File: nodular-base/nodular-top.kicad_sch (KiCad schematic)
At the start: 0 parts

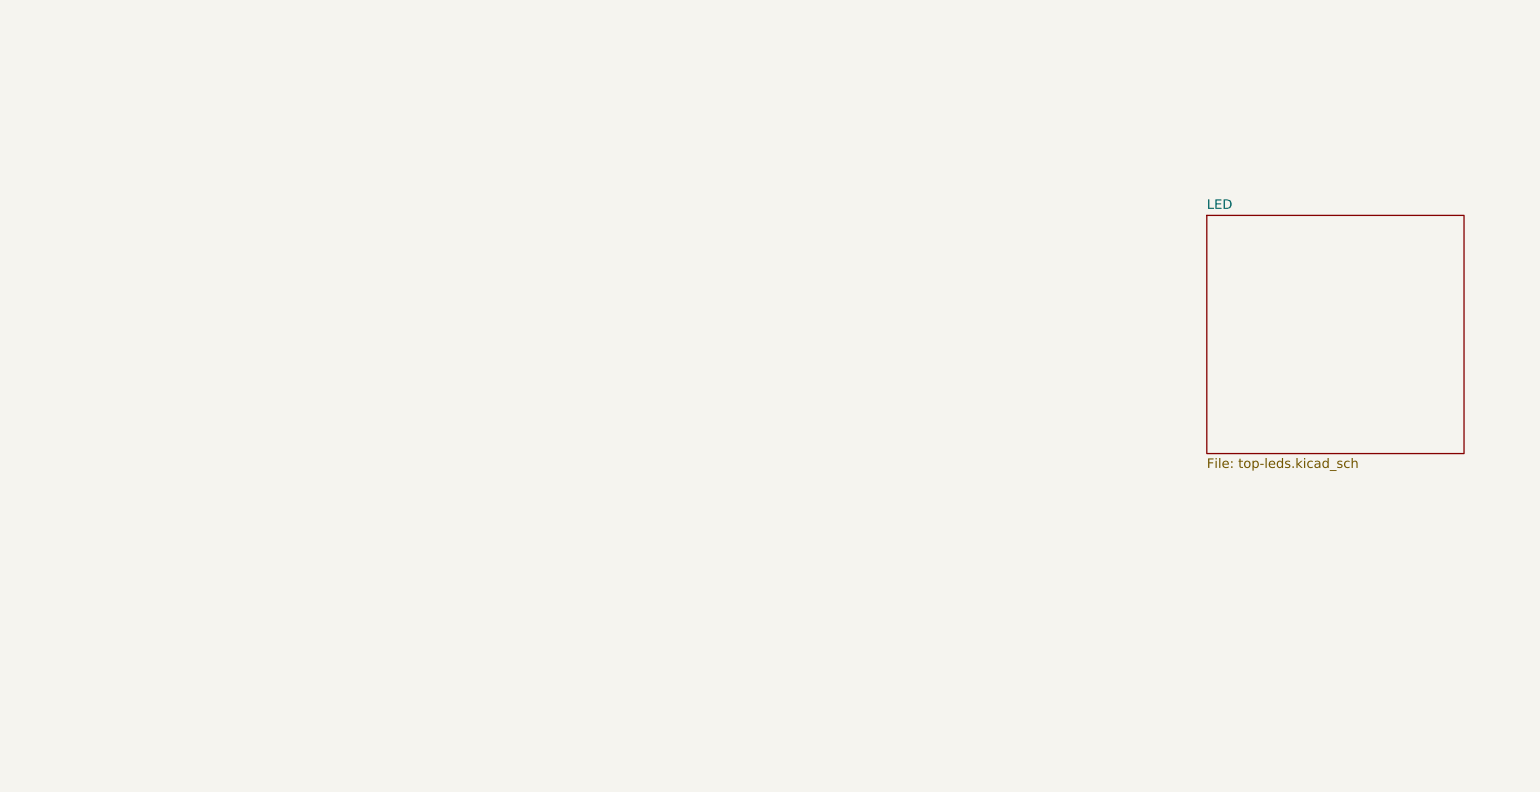
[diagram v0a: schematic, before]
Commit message: Update layout for top board, add library items
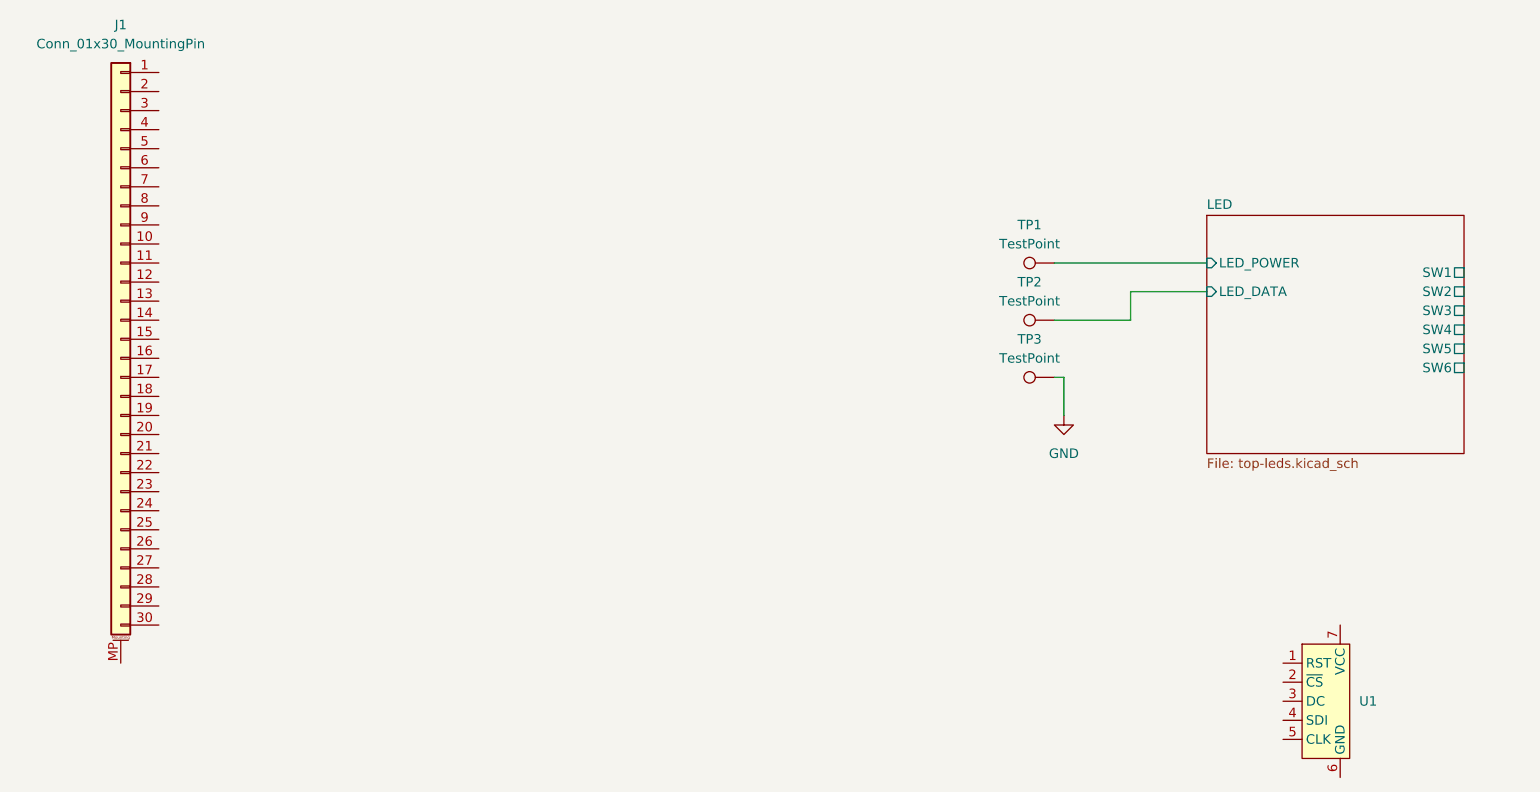
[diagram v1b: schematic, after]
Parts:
- added J1: Conn_01x30_MountingPin, Connector_FFC-FPC:Hirose_FH12-30S-0.5SH_1x30-1MP_P0.50mm_Horizontal, symbol Connector_Generic_MountingPin:Conn_01x30_MountingPin
- added TP1, TP2, TP3: TestPoint, TestPoint:TestPoint_Pad_4.0x4.0mm, symbol Connector:TestPoint
- added U1: ~, nodular:PinHeader_1x07_P2.54mm_Vertical_LockPads, symbol nodular:roundscreen
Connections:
- new net GND: TP3.1
- new net LED/LED_DATA: TP2.1
- new net LED/LED_POWER: TP1.1
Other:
- sheet LED ports: added LED_DATA, LED_POWER, SW1, SW2, SW3, SW4, SW5, SW6; removed none
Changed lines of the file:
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@@
 (kicad_sch (version 20230121) (generator eeschema)
   (paper "A4")
+  (wire (pts (xy 185.42 77.47) (xy 185.42 81.28))
+    (stroke (width 0) (type default))
+  )
+  (wire (pts (xy 195.58 77.47) (xy 185.42 77.47))
+    (stroke (width 0) (type default))
+  )
+  (wire (pts (xy 175.26 88.9) (xy 176.53 88.9))
+    (stroke (width 0) (type default))
+  )
+  (wire (pts (xy 175.26 73.66) (xy 195.58 73.66))
+    (stroke (width 0) (type default))
+  )
+  (wire (pts (xy 185.42 81.28) (xy 175.26 81.28))
+    (stroke (width 0) (type default))
+  )
+  (wire (pts (xy 176.53 88.9) (xy 176.53 93.98))
+    (stroke (width 0) (type default))
+  )
+  (symbol (lib_id "Connector:TestPoint") (at 175.26 88.9 90) (unit 1)
+    (in_bom yes) (on_board yes) (dnp no) (fields_autoplaced)
+    (property "Reference" "TP3" (at 171.958 83.82 90)
+      (effects (font (size 1.27 1.27)))
+    )
+    (property "Value" "TestPoint" (at 171.958 86.36 90)
+      (effects (font (size 1.27 1.27)))
+    )
+    (property "Footprint" "TestPoint:TestPoint_Pad_4.0x4.0mm" (at 175.26 83.82 0)
+      (effects (font (size 1.27 1.27)) hide)
+    )
+    (property "Datasheet" "~" (at 175.26 83.82 0)
+      (effects (font (size 1.27 1.27)) hide)
+    )
+    (pin "1")
+    (instances
+      (project "nodular-top"
+        (path "/67223bb4-fb4b-4d28-a5c8-1b64a0b88fc4"
+          (reference "TP3") (unit 1)
+        )
+      )
+    )
+  )
+  (symbol (lib_id "Connector:TestPoint") (at 175.26 73.66 90) (unit 1)
+    (in_bom yes) (on_board yes) (dnp no) (fields_autoplaced)
+    (property "Reference" "TP1" (at 171.958 68.58 90)
+      (effects (font (size 1.27 1.27)))
+    )
+    (property "Value" "TestPoint" (at 171.958 71.12 90)
+      (effects (font (size 1.27 1.27)))
+    )
+    (property "Footprint" "TestPoint:TestPoint_Pad_4.0x4.0mm" (at 175.26 68.58 0)
+      (effects (font (size 1.27 1.27)) hide)
+    )
+    (property "Datasheet" "~" (at 175.26 68.58 0)
+      (effects (font (size 1.27 1.27)) hide)
+    )
+    (pin "1")
+    (instances
+      (project "nodular-top"
+        (path "/67223bb4-fb4b-4d28-a5c8-1b64a0b88fc4"
+          (reference "TP1") (unit 1)
+        )
+      )
+    )
+  )
+  (symbol (lib_id "power:GND") (at 176.53 93.98 0) (unit 1)
+    (in_bom yes) (on_board yes) (dnp no) (fields_autoplaced)
+    (property "Reference" "#PWR04" (at 176.53 100.33 0)
+      (effects (font (size 1.27 1.27)) hide)
+    )
+    (property "Value" "GND" (at 176.53 99.06 0)
+      (effects (font (size 1.27 1.27)))
+    )
+    (property "Footprint" "" (at 176.53 93.98 0)
+      (effects (font (size 1.27 1.27)) hide)
+    )
+    (property "Datasheet" "" (at 176.53 93.98 0)
+      (effects (font (size 1.27 1.27)) hide)
+    )
+    (pin "1")
+    (instances
+      (project "nodular-top"
+        (path "/67223bb4-fb4b-4d28-a5c8-1b64a0b88fc4"
+          (reference "#PWR04") (unit 1)
+        )
+      )
+    )
+  )
+  (symbol (lib_id "nodular:roundscreen") (at 213.36 132.08 0) (unit 1)
+    (in_bom yes) (on_board yes) (dnp no) (fields_autoplaced)
+    (property "Reference" "U1" (at 215.9 132.08 0)
+      (effects (font (size 1.27 1.27)) (justify left))
+    )
+    (property "Value" "~" (at 213.36 132.08 0)
+      (effects (font (size 1.27 1.27)))
+    )
+    (property "Footprint" "nodular:PinHeader_1x07_P2.54mm_Vertical_LockPads" (at 213.36 132.08 0)
+      (effects (font (size 1.27 1.27)) hide)
+    )
+    (property "Datasheet" "" (at 213.36 132.08 0)
+      (effects (font (size 1.27 1.27)) hide)
+    )
+    (pin "6")
+    (pin "7")
+    (pin "4")
+    (pin "2")
+    (pin "5")
+    (pin "1")
+    (pin "3")
+    (instances
+      (project "nodular-top"
+        (path "/67223bb4-fb4b-4d28-a5c8-1b64a0b88fc4"
+          (reference "U1") (unit 1)
+        )
+      )
+    )
+  )
+  (symbol (lib_id "Connector_Generic_MountingPin:Conn_01x30_MountingPin") (at 50.8 83.82 0) (mirror y) (unit 1)
+    (in_bom yes) (on_board yes) (dnp no) (fields_autoplaced)
+    (property "Reference" "J1" (at 50.8 41.91 0)
+      (effects (font (size 1.27 1.27)))
+    )
+    (property "Value" "Conn_01x30_MountingPin" (at 50.8 44.45 0)
+      (effects (font (size 1.27 1.27)))
+    )
+    (property "Footprint" "Connector_FFC-FPC:Hirose_FH12-30S-0.5SH_1x30-1MP_P0.50mm_Horizontal" (at 50.8 83.82 0)
+      (effects (font (size 1.27 1.27)) hide)
+    )
+    (property "Datasheet" "~" (at 50.8 83.82 0)
+      (effects (font (size 1.27 1.27)) hide)
+    )
+    (pin "7")
+    (pin "29")
+    (pin "28")
+    (pin "25")
+    (pin "17")
+    (pin "6")
+    (pin "8")
+    (pin "23")
+    (pin "MP")
+    (pin "27")
+    (pin "5")
+    (pin "16")
+    (pin "11")
+    (pin "10")
+    (pin "30")
+    (pin "20")
+    (pin "13")
+    (pin "12")
+    (pin "22")
+    (pin "21")
+    (pin "19")
+    (pin "24")
+    (pin "2")
+    (pin "1")
+    (pin "18")
+    (pin "26")
+    (pin "3")
+    (pin "9")
+    (pin "4")
+    (pin "15")
+    (pin "14")
+    (instances
+      (project "nodular-top"
+        (path "/67223bb4-fb4b-4d28-a5c8-1b64a0b88fc4"
+          (reference "J1") (unit 1)
+        )
+      )
+    )
+  )
+  (symbol (lib_id "Connector:TestPoint") (at 175.26 81.28 90) (unit 1)
+    (in_bom yes) (on_board yes) (dnp no) (fields_autoplaced)
+    (property "Reference" "TP2" (at 171.958 76.2 90)
+      (effects (font (size 1.27 1.27)))
+    )
+    (property "Value" "TestPoint" (at 171.958 78.74 90)
+      (effects (font (size 1.27 1.27)))
+    )
+    (property "Footprint" "TestPoint:TestPoint_Pad_4.0x4.0mm" (at 175.26 76.2 0)
+      (effects (font (size 1.27 1.27)) hide)
+    )
+    (property "Datasheet" "~" (at 175.26 76.2 0)
+      (effects (font (size 1.27 1.27)) hide)
+    )
+    (pin "1")
+    (instances
+      (project "nodular-top"
+        (path "/67223bb4-fb4b-4d28-a5c8-1b64a0b88fc4"
+          (reference "TP2") (unit 1)
+        )
+      )
+    )
+  )
   (sheet (at 195.58 67.31) (size 34.29 31.75) (fields_autoplaced)
     (stroke (width 0.1524) (type solid))
@@
       (effects (font (size 1.27 1.27)) (justify left top))
     )
-    (instances
+    (pin "LED_POWER" input (at 195.58 73.66 180)
+      (effects (font (size 1.27 1.27)) (justify left))
+    )
+    (pin "LED_DATA" input (at 195.58 77.47 180)
+      (effects (font (size 1.27 1.27)) (justify left))
+    )
+    (pin "SW5" passive (at 229.87 85.09 0)
+      (effects (font (size 1.27 1.27)) (justify right))
+    )
+    (pin "SW6" passive (at 229.87 87.63 0)
+      (effects (font (size 1.27 1.27)) (justify right))
+    )
+    (pin "SW1" passive (at 229.87 74.93 0)
+      (effects (font (size 1.27 1.27)) (justify right))
+    )
+    (pin "SW2" passive (at 229.87 77.47 0)
+      (effects (font (size 1.27 1.27)) (justify right))
+    )
+    (pin "SW3" passive (at 229.87 80.01 0)
+      (effects (font (size 1.27 1.27)) (justify right))
+    )
+    (pin "SW4" passive (at 229.87 82.55 0)
+      (effects (font (size 1.27 1.27)) (justify right))
+    )
+    (instances
